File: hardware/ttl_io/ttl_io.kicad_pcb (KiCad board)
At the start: 4 copper layers, 120 x 75 mm, 197 parts, among them J1 Conn_01x03_Male, J10 Conn_Coaxial, J11 Conn_Coaxial, J12 Conn_Coaxial, J13 Conn_02x08_Counter_Clockwise, J14 Conn_02x08_Counter_Clockwise, J2 AudioJack3, J3 USB_C_Receptacle_USB2.0, J4 Barrel_Jack_Switch, J5 Conn_Coaxial, J6 Conn_Coaxial, J7 Conn_Coaxial, J8 Conn_Coaxial, J9 Conn_Coaxial, SW2 SW_SPDT, SW3 SW_SPDT, U1 TPD2EUSB30, U10 74LVCH2T45DC, U11 74LVCH2T45DC, U12 74LVCH2T45DC, U13 74LVCH2T45DC, U14 74CBTLV3245, U15 SN74LVC1G14DRL, U16 74CBTLV3245, U17 74CBTLV3245, U18 SN74LVC1G14DRL, U19 TXB0108, U2 ADUM4160, U3 RP2040, U4 W25Q16JVUXIQ, U5 74LVCH2T45DC, U6 74LVCH2T45DC, U7 74LVCH2T45DC, U8 LT3506, U9 74LVCH2T45DC, X1 ECS-TXO-2016

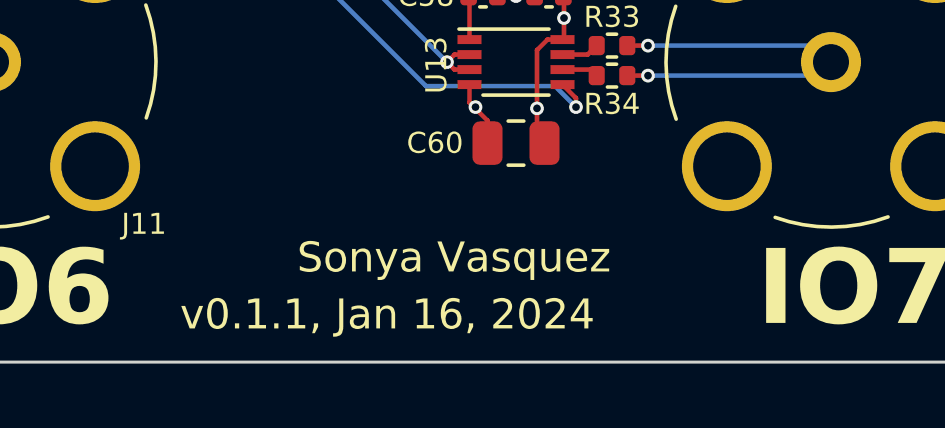
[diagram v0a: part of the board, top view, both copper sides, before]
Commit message: implement finite pulses
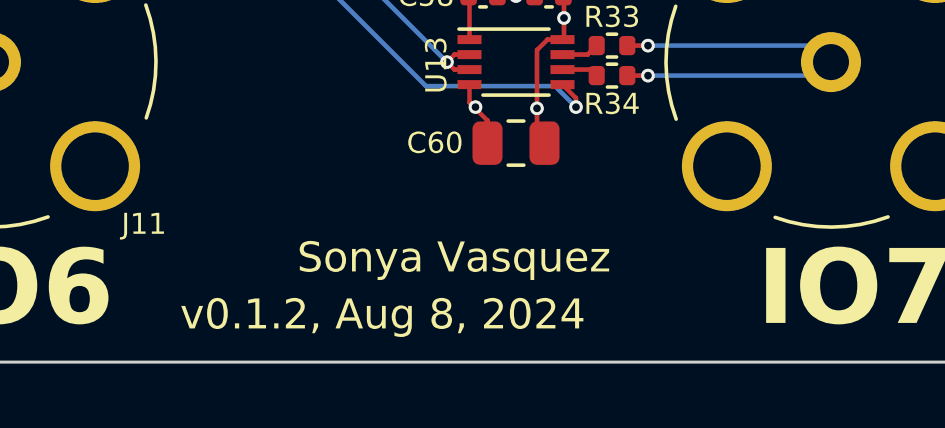
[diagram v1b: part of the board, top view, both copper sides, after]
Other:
- board text added: "USB I/O ↑ ↓ Ext I/O"
- board text added: "v0.1.2, Aug 8, 2024"
- board text removed: "Ext I/O ↑ ↓ USB I/O"
- board text removed: "v0.1.1, Jan 16, 2024"
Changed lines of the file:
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@@
     (effects (font (size 1 1) (thickness 0.2) bold) (justify left bottom mirror))
   )
-  (gr_text "Ext I/O\n↑\n↓\nUSB I/O\n" (at 222.4 59) (layer "B.SilkS")
+  (gr_text "USB I/O\n↑\n↓\nExt I/O" (at 222.4 59) (layer "B.SilkS")
     (effects (font (size 1 1) (thickness 0.2) bold) (justify left bottom mirror))
   )
@@
     (effects (font (size 2.5 2.5) (thickness 0.4) italic) (justify bottom))
   )
-  (gr_text "v0.1.1, Jan 16, 2024" (at 185.2 117) (layer "F.SilkS")
+  (gr_text "v0.1.2, Aug 8, 2024" (at 185.2 117) (layer "F.SilkS")
     (effects (font (size 1 1) (thickness 0.15)) (justify left bottom))
   )

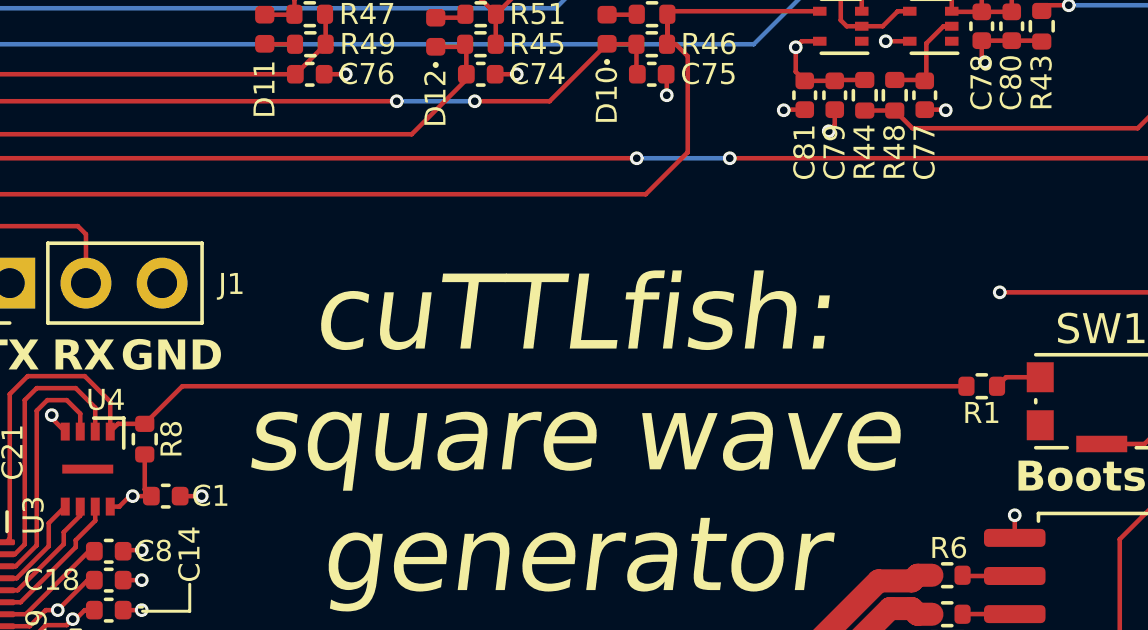
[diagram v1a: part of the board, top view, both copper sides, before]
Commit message: get pwm task and ios working
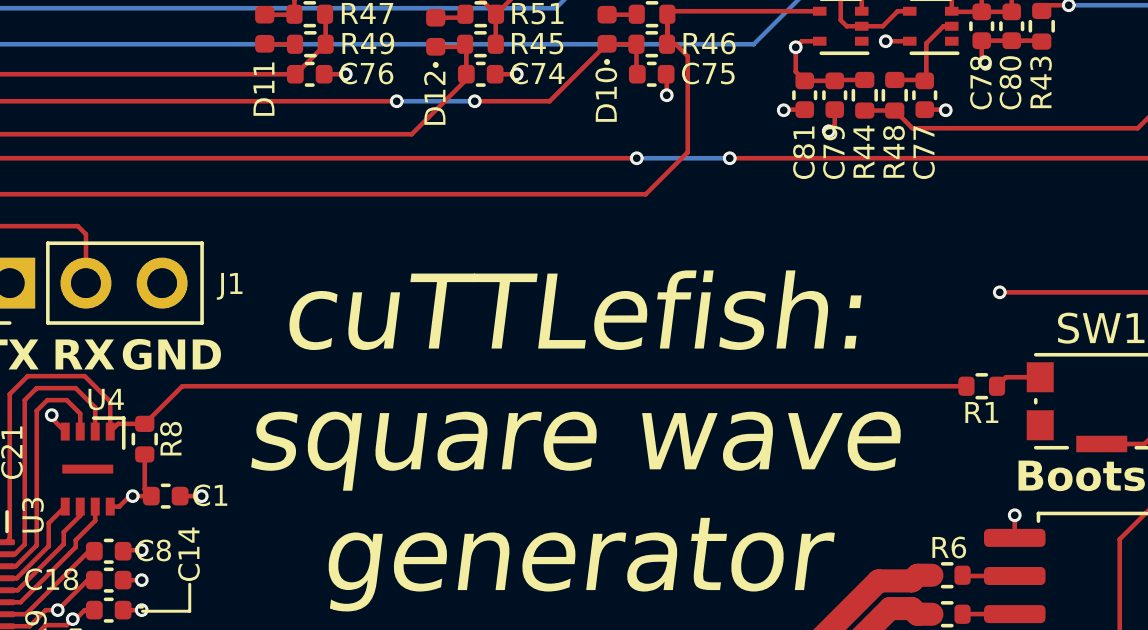
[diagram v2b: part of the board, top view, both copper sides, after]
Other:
- board text added: "cuTTLefish: square wave generator"
- board text removed: "cuTTLfish: square wave generator"
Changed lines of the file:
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@@
     (effects (font (size 1 1) (thickness 0.15)) (justify left bottom))
   )
-  (gr_text "cuTTLfish:\nsquare wave\ngenerator" (at 187.4 79.8) (layer "F.SilkS")
+  (gr_text "cuTTLefish:\nsquare wave\ngenerator" (at 187.4 79.8) (layer "F.SilkS")
     (effects (font (size 2.5 2.5) (thickness 0.4) italic) (justify bottom))
   )
